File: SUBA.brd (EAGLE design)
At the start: 85 x 70 mm, 19 parts, among them J3 PH_A_T, T1 2N2222

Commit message: Algumas alterações PCB
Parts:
- moved J6 23.7 mm to (41.4, 57.0), turned to 270 degrees
- moved PH_A_H 22.2 mm to (55.0, 63.0)
- moved PH_B_H 15.5 mm to (49.9, 26.5)
- moved PH_B_T 12.1 mm to (71.6, -4.70)
- moved J3 12.0 mm to (43.0, -1.00)
- moved JP1 8.44 mm to (39.4, 35.2), turned to 270 degrees
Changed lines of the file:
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@@
 <setting verticaltext="up"/>
 </settings>
-<grid distance="1" unitdist="mm" unit="mm" style="dots" multiple="1" display="no" altdistance="0.01" altunitdist="mm" altunit="mm"/>
+<grid distance="2" unitdist="mm" unit="mm" style="dots" multiple="1" display="no" altdistance="0.01" altunitdist="mm" altunit="mm"/>
 <layers>
 <layer number="1" name="Top" color="4" fill="1" visible="yes" active="yes"/>
@@
 <attribute name="SF_SKU" value="PRT-08433" x="18.51" y="8.16" size="1.778" layer="27" rot="R180" display="off"/>
 </element>
-<element name="J3" library="SparkFun-Connectors" package="SCREWTERMINAL-5MM-2" value="PH_A_T" x="52" y="7" rot="R180">
-<attribute name="SF_SKU" value="PRT-08432" x="52" y="7" size="1.778" layer="27" rot="R180" display="off"/>
-</element>
-<element name="JP1" library="pinhead" package="1X04" value="PH_PWM_H" x="31.17" y="36.98" rot="R90"/>
+<element name="J3" library="SparkFun-Connectors" package="SCREWTERMINAL-5MM-2" value="PH_A_T" x="43" y="-1" rot="R180">
+<attribute name="SF_SKU" value="PRT-08432" x="43" y="-1" size="1.778" layer="27" rot="R180" display="off"/>
+</element>
+<element name="JP1" library="pinhead" package="1X04" value="PH_PWM_H" x="39.42" y="35.21" rot="R270"/>
 <element name="JP2" library="pinhead" package="1X04" value="BT" x="37.55" y="5.83"/>
 <element name="JP7" library="pinhead" package="1X12" value="Arduino_1_B" x="19.76" y="52.8" rot="R90"/>
 <element name="JP8" library="pinhead" package="1X12" value="Arduino_2_C" x="7.06" y="52.8" rot="R90"/>
-<element name="PH_B_T" library="SparkFun-Connectors" package="SCREWTERMINAL-5MM-2" value="" x="66.59" y="6.3" rot="R180">
-<attribute name="SF_SKU" value="PRT-08432" x="66.59" y="6.3" size="1.778" layer="27" rot="R180" display="off"/>
+<element name="PH_B_T" library="SparkFun-Connectors" package="SCREWTERMINAL-5MM-2" value="" x="71.59" y="-4.7" rot="R180">
+<attribute name="SF_SKU" value="PRT-08432" x="71.59" y="-4.7" size="1.778" layer="27" rot="R180" display="off"/>
 </element>
 <element name="R1" library="eagle-ltspice" package="0204/7" value="1KR" x="33.09" y="15.44" rot="R90">
@@
 </element>
 <element name="SERVO" library="SparkFun-Connectors" package="1X03" value="" x="6" y="27" rot="R90"/>
-<element name="J6" library="SparkFun-Connectors" package="1X05" value="" x="65" y="59"/>
-<element name="PH_A_H" library="SparkFun-Connectors" package="1X03" value="" x="58" y="41" rot="R180"/>
-<element name="PH_B_H" library="SparkFun-Connectors" package="1X03" value="" x="65" y="30"/>
+<element name="J6" library="SparkFun-Connectors" package="1X05" value="" x="41.42" y="57.01" rot="R270"/>
+<element name="PH_A_H" library="SparkFun-Connectors" package="1X03" value="" x="55" y="63" rot="R180"/>
+<element name="PH_B_H" library="SparkFun-Connectors" package="1X03" value="" x="49.92" y="26.5"/>
 </elements>
 <signals>
@@
 <contactref element="JP1" pad="4"/>
 <contactref element="JP8" pad="7"/>
-<wire x1="7.06" y1="54.07" x2="31.17" y2="40.79" width="0" layer="19" extent="1-1"/>
+<wire x1="7.06" y1="54.07" x2="39.42" y2="31.4" width="0" layer="19" extent="1-1"/>
 </signal>
 <signal name="IN3">
 <contactref element="JP1" pad="3"/>
 <contactref element="JP8" pad="5"/>
-<wire x1="7.06" y1="48.99" x2="31.17" y2="38.25" width="0" layer="19" extent="1-1"/>
+<wire x1="7.06" y1="48.99" x2="39.42" y2="33.94" width="0" layer="19" extent="1-1"/>
 </signal>
 <signal name="IN2">
 <contactref element="JP1" pad="2"/>
 <contactref element="JP8" pad="4"/>
-<wire x1="31.17" y1="35.71" x2="7.06" y2="46.45" width="0" layer="19" extent="1-1"/>
+<wire x1="39.42" y1="36.48" x2="7.06" y2="46.45" width="0" layer="19" extent="1-1"/>
 </signal>
 <signal name="IN1">
 <contactref element="JP1" pad="1"/>
 <contactref element="JP8" pad="1"/>
-<wire x1="31.17" y1="33.17" x2="7.06" y2="38.83" width="0" layer="19" extent="1-1"/>
+<wire x1="39.42" y1="39.02" x2="7.06" y2="38.83" width="0" layer="19" extent="1-1"/>
 </signal>
 <signal name="12V">
@@
 <contactref element="J5" pad="1"/>
 <contactref element="J6" pad="1"/>
-<wire x1="8.51" y1="8.16" x2="65" y2="59" width="0" layer="19" extent="1-1"/>
+<wire x1="8.51" y1="8.16" x2="41.42" y2="57.01" width="0" layer="19" extent="1-1"/>
 <wire x1="8.82" y1="15.37" x2="8.51" y2="8.16" width="0" layer="19" extent="1-1"/>
 <wire x1="11.36" y1="15.37" x2="8.82" y2="15.37" width="0" layer="19" extent="1-1"/>
@@
 <contactref element="J3" pad="1"/>
 <contactref element="PH_A_H" pad="1"/>
-<wire x1="52" y1="7" x2="58" y2="41" width="0" layer="19" extent="1-1"/>
+<wire x1="43" y1="-1" x2="55" y2="63" width="0" layer="19" extent="1-1"/>
 </signal>
 <signal name="N$10">
 <contactref element="PH_B_T" pad="1"/>
 <contactref element="PH_B_H" pad="3"/>
-<wire x1="66.59" y1="6.3" x2="70.08" y2="30" width="0" layer="19" extent="1-1"/>
+<wire x1="71.59" y1="-4.7" x2="55" y2="26.5" width="0" layer="19" extent="1-1"/>
 </signal>
 <signal name="N$11">
 <contactref element="PH_B_T" pad="2"/>
 <contactref element="PH_B_H" pad="1"/>
-<wire x1="61.59" y1="6.3" x2="65" y2="30" width="0" layer="19" extent="1-1"/>
+<wire x1="66.59" y1="-4.7" x2="49.92" y2="26.5" width="0" layer="19" extent="1-1"/>
 </signal>
 <signal name="TX">
@@
 <wire x1="18.51" y1="8.16" x2="13.9" y2="21.42" width="0" layer="19" extent="1-1"/>
 <wire x1="41.36" y1="5.83" x2="18.51" y2="8.16" width="0" layer="19" extent="1-1"/>
-<wire x1="75.16" y1="59" x2="18.51" y2="8.16" width="0" layer="19" extent="1-1"/>
+<wire x1="41.42" y1="46.85" x2="18.51" y2="8.16" width="0" layer="19" extent="1-1"/>
 </signal>
 <signal name="N$12">
@@
 <wire x1="36.47" y1="11.41" x2="17.74" y2="17.03" width="0" layer="19" extent="1-1"/>
 <wire x1="38.82" y1="5.83" x2="36.47" y2="11.41" width="0" layer="19" extent="1-1"/>
-<wire x1="70.08" y1="59" x2="13.51" y2="8.16" width="0" layer="19" extent="1-1"/>
+<wire x1="41.42" y1="51.93" x2="13.51" y2="8.16" width="0" layer="19" extent="1-1"/>
 </signal>
 <signal name="RX">
@@
 <contactref element="J3" pad="2"/>
 <contactref element="PH_A_H" pad="3"/>
-<wire x1="47" y1="7" x2="52.92" y2="41" width="0" layer="19" extent="1-1"/>
+<wire x1="38" y1="-1" x2="49.92" y2="63" width="0" layer="19" extent="1-1"/>
 </signal>
 </signals>

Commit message: SAFE
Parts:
- moved J3 14.4 mm to (55.0, 7.00)
- moved PH_B_T 12.2 mm to (68.0, 7.00)
- moved R3 11.6 mm to (42.1, 15.4)
- moved SERVO 11.1 mm to (6.27, 15.9)
- moved JP7 10.6 mm to (23.3, 42.8)
- moved JP8 10.0 mm to (7.06, 42.8)
- moved J2 5.00 mm to (11.3, 18.5)
- moved J4 5.00 mm to (11.3, 21.4)
- moved J5 5.00 mm to (11.3, 15.4)
- moved T1 3.42 mm to (23.7, 18.3), turned to 90 degrees
- moved R2 1.64 mm to (38.1, 15.4)
- moved LED_STRIP 1.00 mm to (25.5, 6.28)
- moved R1 1.00 mm to (34.1, 15.4)
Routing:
- net N$15: track 310.0 -> 0.00 mm
- added copper zone on layer 1, net N$15
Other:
- board size 85 x 70 mm -> 85 x 67 mm
- board text added: "1234567 tiratirametemete"
- board text added: "12V GND VCC"
- board text added: "2K17"
- board text added: "AREDJUINO"
- board text added: "Copycats wil be prostituted"
- board text added: "Este projecto use um ardjuino"
- board text added: "LED GND 12V"
- board text added: "Powered by AM & NMM"

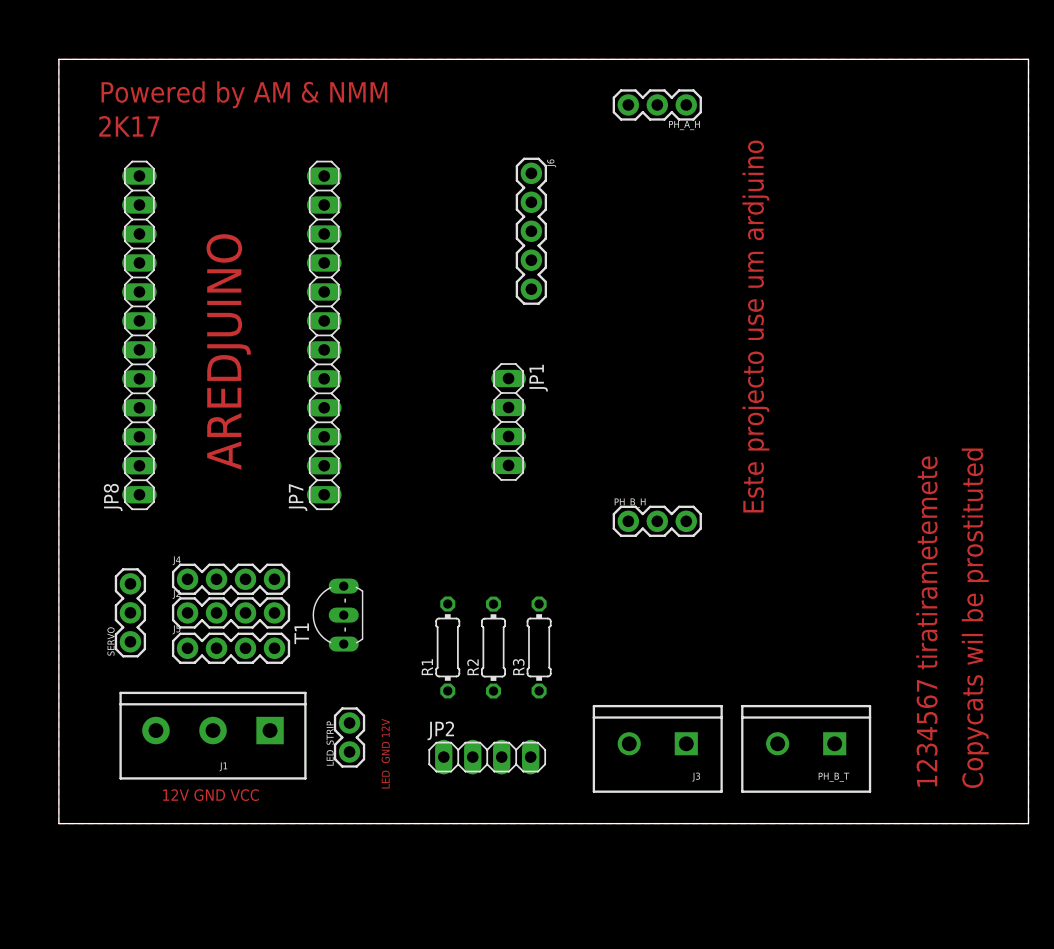
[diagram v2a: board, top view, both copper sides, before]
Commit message: Placed Unrouted
Placed all components, no routing
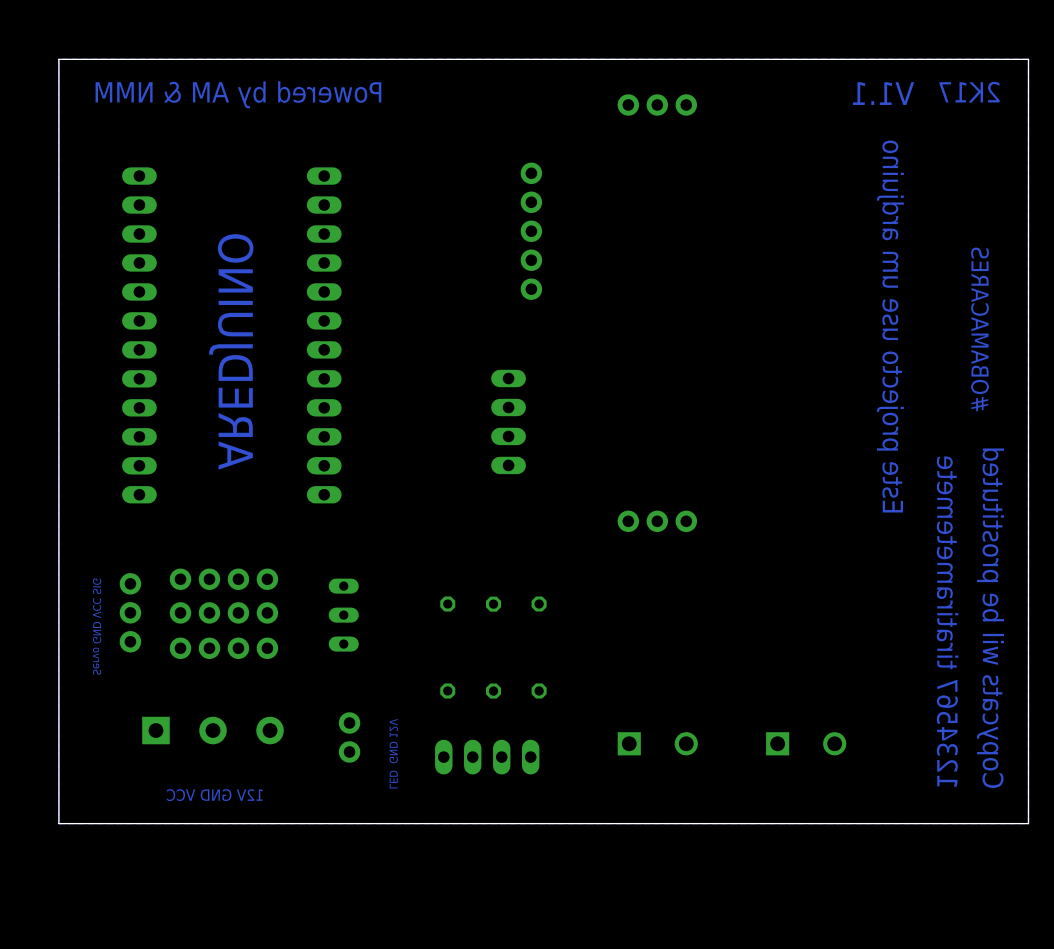
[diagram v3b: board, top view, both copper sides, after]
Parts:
- moved J1 10.0 mm to (8.51, 8.16), flipped to the bottom
- moved J2 7.00 mm to (18.3, 18.5), flipped to the bottom
- moved J4 7.00 mm to (18.3, 21.4), flipped to the bottom
- moved J5 7.00 mm to (18.3, 15.4), flipped to the bottom
- moved PH_B_T 5.00 mm to (63.0, 7.00), flipped to the bottom
- moved J3 5.00 mm to (50.0, 7.00), flipped to the bottom
- flipped J6 to the bottom
- flipped JP1 to the bottom
- flipped JP2 to the bottom, turned to 180 degrees
- flipped JP7 to the bottom
- flipped JP8 to the bottom
- flipped LED_STRIP to the bottom
- flipped PH_A_H to the bottom, turned to 0 degrees
- flipped PH_B_H to the bottom, turned to 180 degrees
- flipped R1 to the bottom
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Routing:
- added copper zone on layer 16, net N$15
- removed copper zone on layer 1, net N$15
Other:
- board text added: "#OBAMACARES"
- board text added: "Servo GND VCC SIG"
- board text added: "V1.1"

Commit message: 100%Routed
WOOO!
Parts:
- moved JP8 19.9 mm to (26.9, 44.2), turned to 270 degrees
- moved JP7 12.6 mm to (10.7, 44.2), turned to 270 degrees
- moved R1 6.08 mm to (33.1, 21.4)
- moved R3 6.08 mm to (43.1, 21.4)
- moved J4 6.00 mm to (18.3, 15.4)
- moved J5 6.00 mm to (18.3, 21.4)
- moved SERVO 5.14 mm to (6.73, 21.1), turned to 270 degrees
- moved R2 2.38 mm to (38.6, 13.1), turned to 0 degrees
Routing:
- net VCC: track 0.00 -> 182.1 mm
- net GND: track 0.00 -> 139.0 mm
- net N$2: track 0.00 -> 110.7 mm
- net 12V: track 0.00 -> 97.2 mm
- net N$9: track 0.00 -> 84.3 mm
- net N$1: track 0.00 -> 69.3 mm
- net N$18: track 0.00 -> 45.6 mm
- net RX: track 0.00 -> 41.2 mm
- net TX: track 0.00 -> 39.5 mm
- net N$11: track 0.00 -> 34.3 mm
- net N$13: track 0.00 -> 32.0 mm
- net IN1: track 0.00 -> 25.2 mm
- net N$21: track 0.00 -> 24.4 mm
- net IN2: track 0.00 -> 23.9 mm
- net N$10: track 0.00 -> 23.1 mm
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
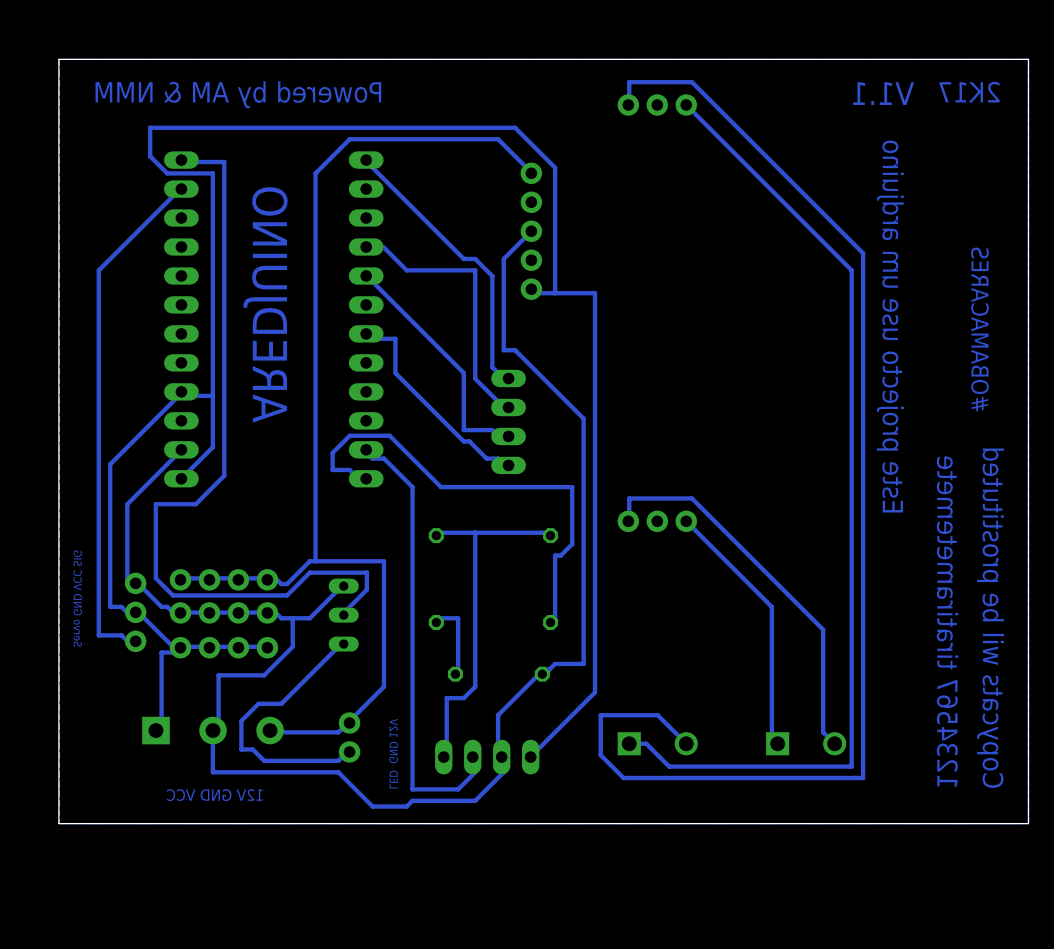
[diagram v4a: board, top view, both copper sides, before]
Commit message: 100% Routed, more spacing
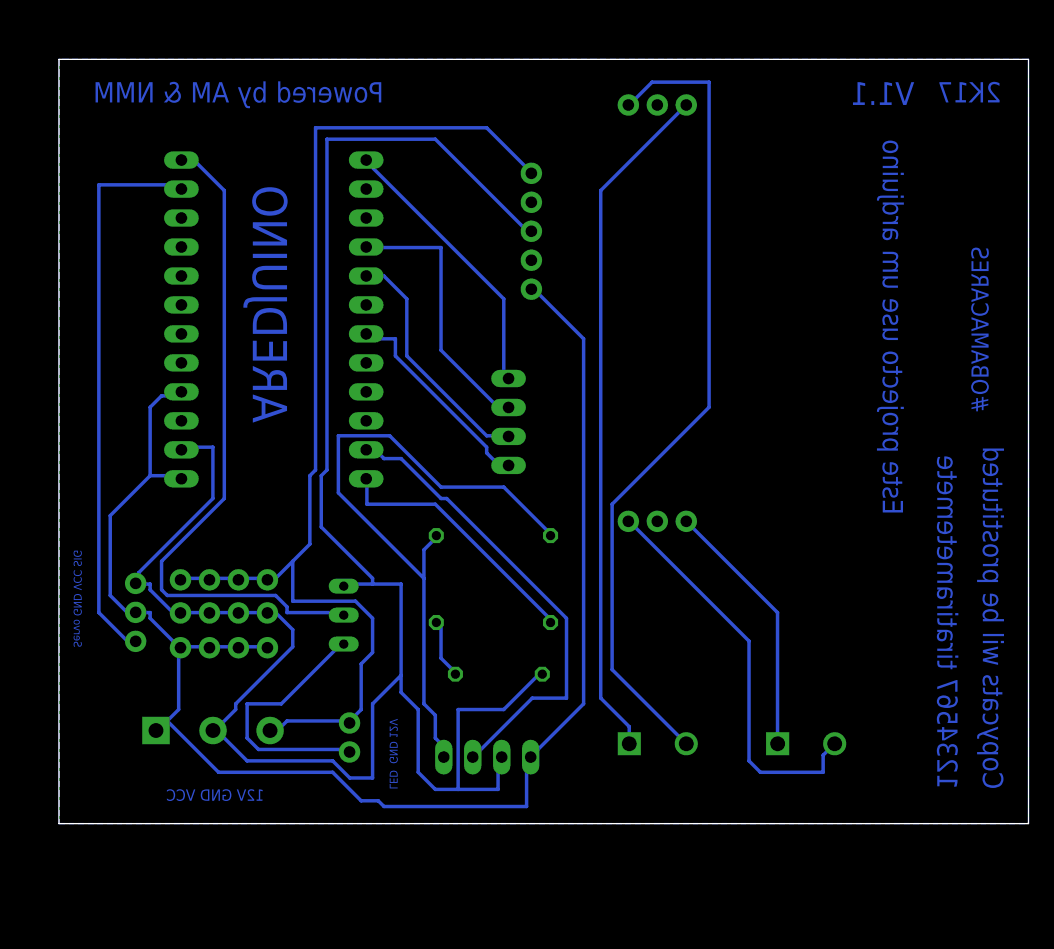
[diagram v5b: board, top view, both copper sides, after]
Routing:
- net VCC: track 182.1 -> 134.1 mm
- net GND: track 139.0 -> 182.2 mm
- net N$2: track 110.7 -> 72.1 mm
- net N$13: track 32.0 -> 58.5 mm
- net N$9: track 84.3 -> 60.1 mm
- net RX: track 41.2 -> 22.8 mm
- net N$1: track 69.3 -> 59.3 mm
- net N$18: track 45.6 -> 49.7 mm
- net 12V: track 97.2 -> 99.1 mm
- net N$12: track 7.02 -> 5.32 mm
- net TX: track 39.5 -> 41.1 mm
- net N$21: track 24.4 -> 23.0 mm
- net N$11: track 34.3 -> 35.3 mm
- net IN1: track 25.2 -> 24.3 mm
